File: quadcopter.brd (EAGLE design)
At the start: 185.1 x 185.1 mm, 66 parts, among them J1 AVR_SPI_PRG_6NS, Q1 2.6A, Q2 2.6A, Q3 2.6A, Q4 2.6A, U1 ATMEGA128RFA1, U2 IMU_LSM9DS1TR, Y1 16MHz

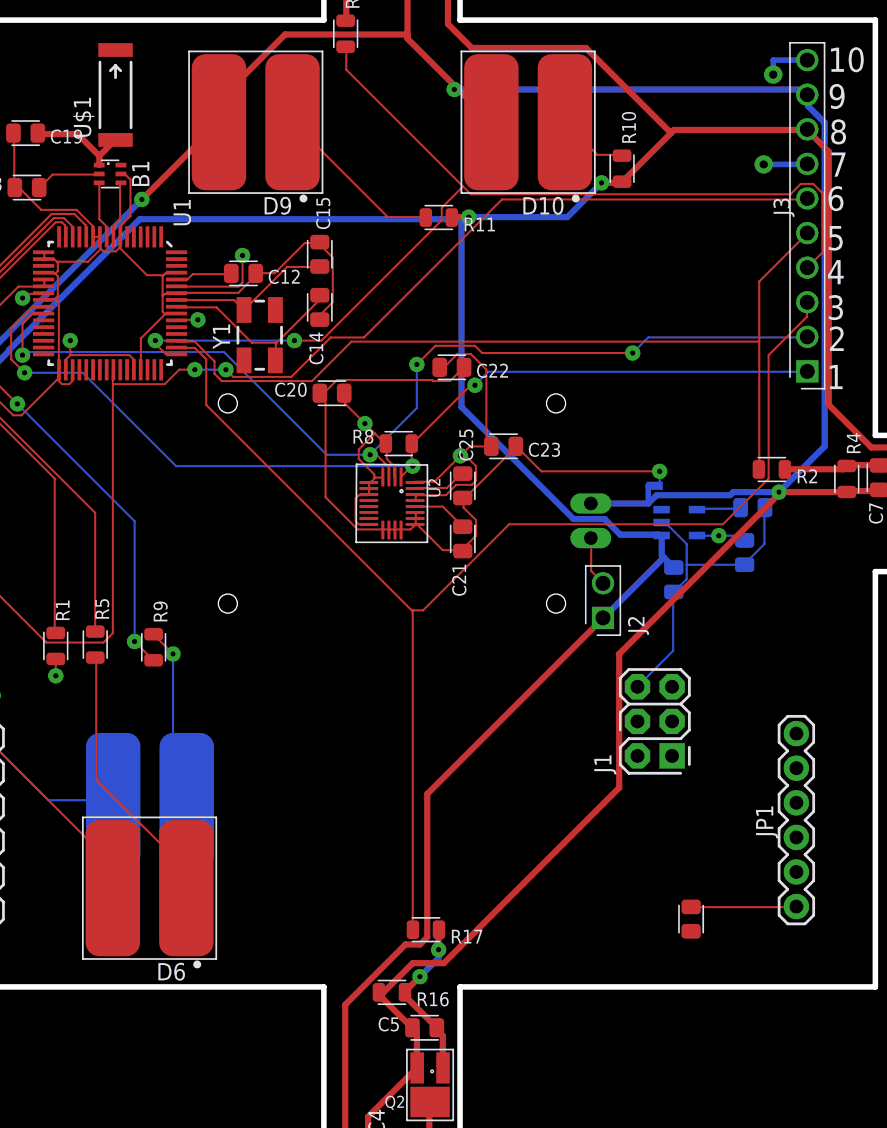
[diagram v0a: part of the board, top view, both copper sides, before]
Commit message: Fixed stop mask errors generated by autorouter
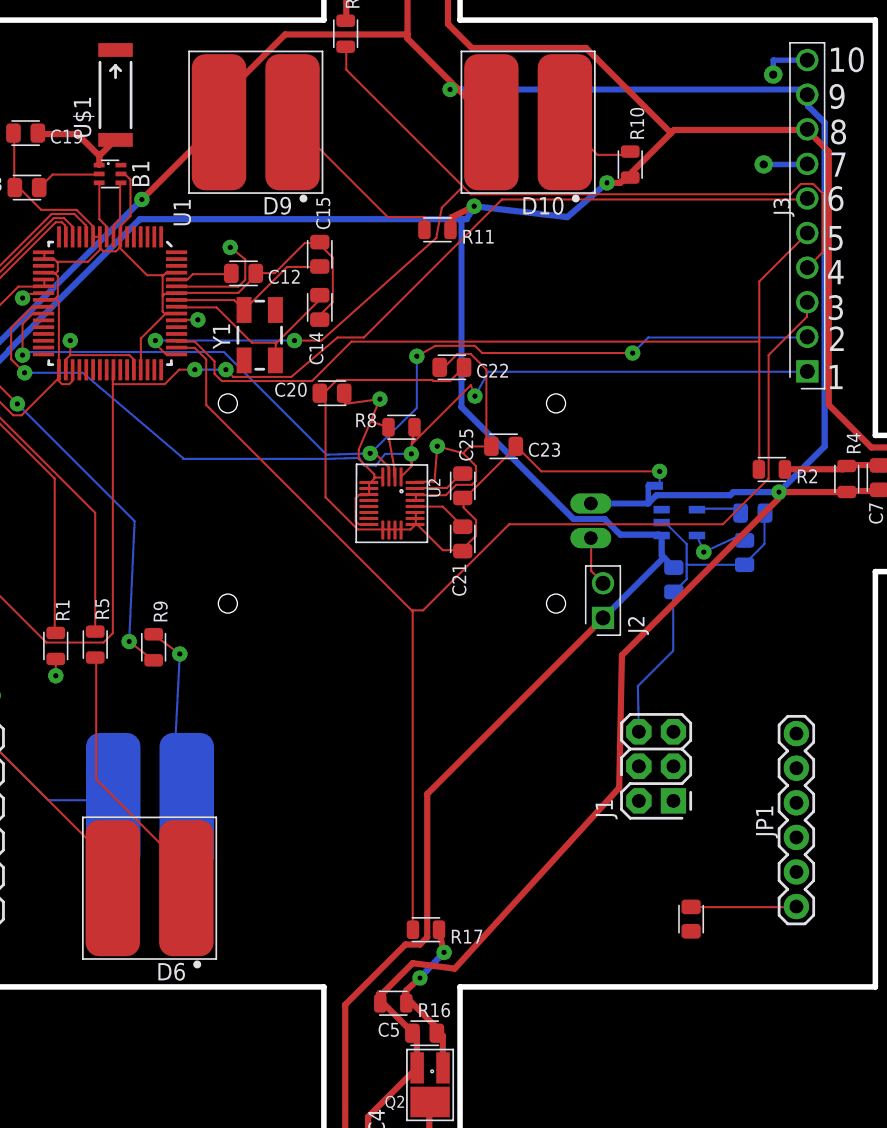
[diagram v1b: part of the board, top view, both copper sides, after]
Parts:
- moved J1 3.30 mm to (19.4, -19.3)
- moved R8 1.22 mm to (0.70, 5.60)
- moved R11 0.91 mm to (3.34, 20.1)
- moved R16 0.81 mm to (0.10, -36.7)
- moved R10 0.67 mm to (17.5, 24.9)
- moved C16 0.40 mm to (26.5, -0.70)
- moved C5 0.40 mm to (2.40, -38.9)
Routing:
- net 3V: track 69.1 -> 76.1 mm
- net SCL: track 72.2 -> 76.6 mm
- net GND: track 195.9 -> 199.6 mm
- net BAT_GND: track 255.6 -> 258.5 mm
- net VBAT: track 319.5 -> 322.3 mm
- net N$34: track 12.3 -> 14.3 mm
- net N$27: track 12.7 -> 13.6 mm
- net N$18: track 5.22 -> 5.84 mm

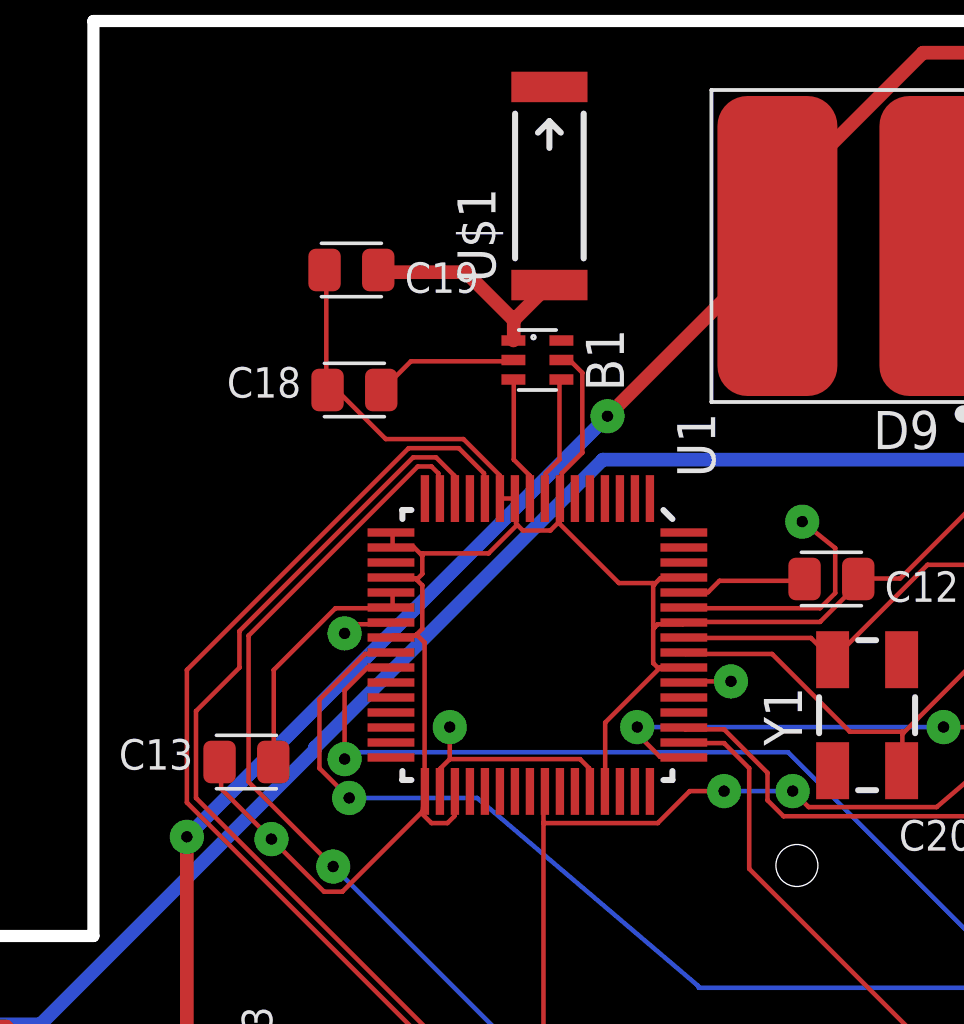
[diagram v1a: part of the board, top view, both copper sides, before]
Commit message: added faraday cage around antenna driver
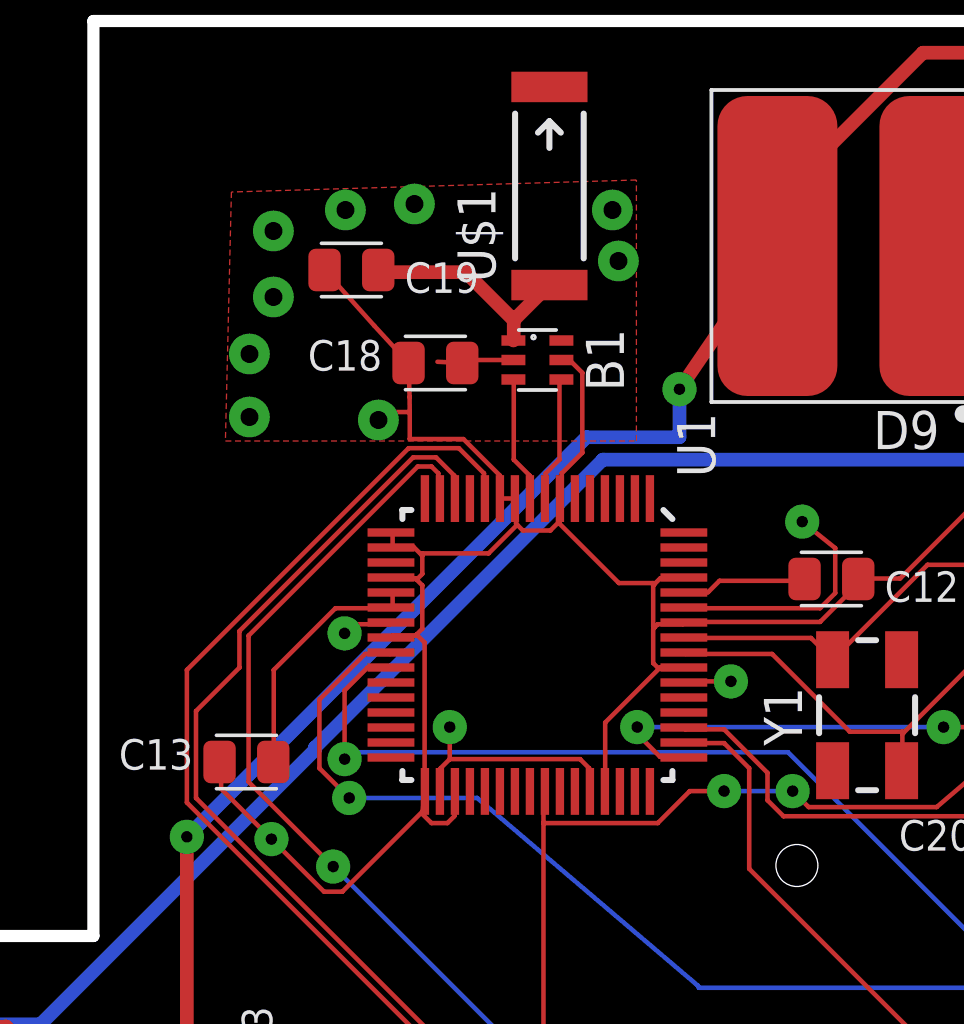
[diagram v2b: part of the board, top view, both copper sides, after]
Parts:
- moved C18 2.85 mm to (-24.1, 24.1)
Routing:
- net N$25: track 4.81 -> 2.63 mm
- net BAT_GND: track 258.5 -> 260.0 mm
- net GND: track 199.6 -> 200.1 mm, vias 4 -> 13
- added copper zone on layer 1, net N$35
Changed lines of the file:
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@@
 <text x="32" y="29" size="1.778" layer="21">9</text>
 <text x="32" y="31.7" size="1.778" layer="21">10</text>
-<polygon width="0.4064" layer="41">
-<vertex x="-34.8" y="33.1"/>
-<vertex x="-17.4" y="32.2"/>
-<vertex x="-17.4" y="28"/>
-<vertex x="-29.1" y="28.6"/>
-<vertex x="-29.1" y="21.5"/>
-<vertex x="-35" y="21.5"/>
-</polygon>
-<polygon width="0.4064" layer="42">
-<vertex x="-17.4" y="32.2"/>
-<vertex x="-17.4" y="28"/>
-<vertex x="-29.1" y="28.6"/>
-<vertex x="-29.1" y="21.4"/>
-<vertex x="-34.9" y="21.4"/>
-<vertex x="-34.8" y="33.1"/>
-</polygon>
-<polygon width="0.4064" layer="41">
-<vertex x="-18.1" y="32.5"/>
-<vertex x="-15.6" y="32.5"/>
-<vertex x="-15.6" y="35"/>
-<vertex x="-18.1" y="35"/>
-</polygon>
-<polygon width="0.4064" layer="41">
-<vertex x="-34.9" y="34.9"/>
-<vertex x="-22.6" y="34.9"/>
-<vertex x="-22.6" y="32.9"/>
-<vertex x="-34.9" y="32.9"/>
-</polygon>
-<polygon width="0.4064" layer="42">
-<vertex x="-18.1" y="35"/>
-<vertex x="-15.5" y="35"/>
-<vertex x="-15.5" y="32.5"/>
-<vertex x="-18.1" y="32.5"/>
-</polygon>
-<polygon width="0.4064" layer="42">
-<vertex x="-34.9" y="34.9"/>
-<vertex x="-22.6" y="34.9"/>
-<vertex x="-22.6" y="32.9"/>
-<vertex x="-34.9" y="32.9"/>
-</polygon>
 </plain>
 <attributes>
@@
 <attribute name="MPN" value="GRM2195C1H103FA01D" x="26.5" y="-0.7" size="1.778" layer="28" rot="MR180" display="off"/>
 </element>
-<element name="C18" library="quadparts_prebuilt" package="CAPC2012X140_HS" value="22pF" x="-26.8" y="23.2" rot="R180">
-<attribute name="DIST" value="Digikey" x="-26.8" y="23.2" size="1.778" layer="27" rot="R180" display="off"/>
-<attribute name="DISTPN" value="490-5534-1-ND" x="-26.8" y="23.2" size="1.778" layer="27" rot="R180" display="off"/>
-<attribute name="MFR" value="Murata Electronics North America" x="-26.8" y="23.2" size="1.778" layer="27" rot="R180" display="off"/>
-<attribute name="MPN" value="GRM21A5C2E220JW01D" x="-26.8" y="23.2" size="1.778" layer="27" rot="R180" display="off"/>
+<element name="C18" library="quadparts_prebuilt" package="CAPC2012X140_HS" value="22pF" x="-24.1" y="24.1" rot="R180">
+<attribute name="DIST" value="Digikey" x="-24.1" y="24.1" size="1.778" layer="27" rot="R180" display="off"/>
+<attribute name="DISTPN" value="490-5534-1-ND" x="-24.1" y="24.1" size="1.778" layer="27" rot="R180" display="off"/>
+<attribute name="MFR" value="Murata Electronics North America" x="-24.1" y="24.1" size="1.778" layer="27" rot="R180" display="off"/>
+<attribute name="MPN" value="GRM21A5C2E220JW01D" x="-24.1" y="24.1" size="1.778" layer="27" rot="R180" display="off"/>
 </element>
 <element name="C19" library="quadparts_prebuilt" package="CAPC2012X140_HS" value="0.75pF" x="-26.9" y="27.2">
@@
 <vertex x="7.5" y="70.6"/>
 <vertex x="-16.4" y="70.6"/>
-<vertex x="-16.9" y="20.8"/>
+<vertex x="-16.5" y="20.8"/>
 </polygon>
 <polygon width="0.4064" layer="2">
-<vertex x="-28.9" y="29.1"/>
-<vertex x="-17.7" y="29.1"/>
-<vertex x="-17.7" y="21.5"/>
-<vertex x="-28.9" y="21.5"/>
+<vertex x="-30.9" y="29.8"/>
+<vertex x="-17.4" y="30.1"/>
+<vertex x="-17.4" y="21.5"/>
+<vertex x="-31.1" y="21.5"/>
 </polygon>
 <wire x1="-31.242" y1="9.906" x2="-31.242" y2="10.7442" width="0.1524" layer="1"/>
@@
 <wire x1="-15.8496" y1="16.9164" x2="-15.819" y2="16.95" width="0.1524" layer="1"/>
 <wire x1="-16.8402" y1="15.3162" x2="-16.8021" y2="15.2781" width="0.1524" layer="1"/>
-<wire x1="-27.7368" y1="23.241" x2="-27.7368" y2="27.1272" width="0.1524" layer="1"/>
+<wire x1="-26.1368" y1="25.341" x2="-27.7368" y2="27.1272" width="0.1524" layer="1"/>
 <wire x1="-27.7368" y1="27.1272" x2="-27.795" y2="27.2" width="0.1524" layer="1"/>
-<wire x1="-27.7368" y1="23.241" x2="-27.695" y2="23.2" width="0.1524" layer="1"/>
+<wire x1="-26.1368" y1="25.341" x2="-24.995" y2="24.1" width="0.1524" layer="1"/>
 <wire x1="-25.527" y1="18.4404" x2="-25.527" y2="17.9832" width="0.1524" layer="1"/>
 <wire x1="-25.527" y1="17.9832" x2="-25.581" y2="17.95" width="0.1524" layer="1"/>
@@
 <wire x1="-21.3741" y1="18.7071" x2="-22.3266" y2="17.7546" width="0.1524" layer="1"/>
 <wire x1="-24.5364" y1="17.7546" x2="-24.5745" y2="17.7165" width="0.1524" layer="1"/>
-<wire x1="-27.3558" y1="23.1648" x2="-27.6606" y2="23.1648" width="0.1524" layer="1"/>
-<wire x1="-25.7556" y1="21.5646" x2="-27.3558" y2="23.1648" width="0.1524" layer="1"/>
-<wire x1="-23.1648" y1="21.5646" x2="-25.7556" y2="21.5646" width="0.1524" layer="1"/>
+<wire x1="-24.9606" y1="22.9648" x2="-24.9558" y2="22.4648" width="0.1524" layer="1"/>
+<wire x1="-24.9556" y1="21.5646" x2="-24.9558" y2="22.4648" width="0.1524" layer="1"/>
+<wire x1="-23.1648" y1="21.5646" x2="-24.9556" y2="21.5646" width="0.1524" layer="1"/>
 <wire x1="-21.9456" y1="20.3454" x2="-23.1648" y2="21.5646" width="0.1524" layer="1"/>
 <wire x1="-21.9456" y1="19.6596" x2="-21.9456" y2="20.3454" width="0.1524" layer="1"/>
-<wire x1="-27.6606" y1="23.1648" x2="-27.695" y2="23.2" width="0.1524" layer="1"/>
+<wire x1="-24.9606" y1="22.9648" x2="-24.995" y2="24.1" width="0.1524" layer="1"/>
 <wire x1="-21.9456" y1="19.6596" x2="-21.95" y2="19.581" width="0.1524" layer="1"/>
 <wire x1="-17.9832" y1="16.764" x2="-16.8402" y2="16.764" width="0.1524" layer="1"/>
@@
 <wire x1="-29.4" y1="-14.1" x2="-29.8" y2="-14" width="0.4064" layer="16"/>
 <wire x1="-29.8" y1="-14" x2="-29.8" y2="-17.2" width="0.4064" layer="16"/>
+<via x="-30.3" y="22.3" extent="1-16" drill="0.6"/>
+<via x="-30.3" y="24.4" extent="1-16" drill="0.6"/>
+<via x="-29.5" y="26.3" extent="1-16" drill="0.6"/>
+<via x="-26" y="22.2" extent="1-16" drill="0.6"/>
+<via x="-18" y="27.5" extent="1-16" drill="0.6"/>
+<via x="-18.2" y="29.2" extent="1-16" drill="0.6"/>
+<via x="-24.8" y="29.4" extent="1-16" drill="0.6"/>
+<via x="-27.1" y="29.2" extent="1-16" drill="0.6"/>
+<via x="-29.5" y="28.5" extent="1-16" drill="0.6"/>
+<wire x1="-24.9558" y1="22.4648" x2="-26" y2="22.4648" width="0.1524" layer="1"/>
+<wire x1="-26" y1="22.4648" x2="-26" y2="22.2" width="0.1524" layer="1"/>
 </signal>
 <signal name="N$2">
@@
 <wire x1="-37.1094" y1="0.6858" x2="-36.95" y2="0.55" width="0.4572" layer="1"/>
 <wire x1="-32.385" y1="8.3058" x2="-32.385" y2="0.1524" width="0.4572" layer="1"/>
-<wire x1="-18.3642" y1="22.3266" x2="-32.385" y2="8.3058" width="0.4572" layer="16"/>
-<wire x1="-12.7254" y1="27.9654" x2="-18.3642" y2="22.3266" width="0.4572" layer="1"/>
+<wire x1="-12.7254" y1="27.9654" x2="-15.9642" y2="23.2266" width="0.4572" layer="1"/>
 <wire x1="-12.7254" y1="27.9654" x2="-12.7" y2="28" width="0.4572" layer="1"/>
 <wire x1="-7.8486" y1="34.4424" x2="1.143" y2="34.4424" width="0.4572" layer="1"/>
@@
 <wire x1="30.3276" y1="30.1752" x2="30.5" y2="30.02" width="0.4572" layer="16"/>
 <via x="-32.385" y="8.3058" extent="1-16" drill="0.381"/>
-<via x="-18.3642" y="22.3266" extent="1-16" drill="0.381"/>
+<via x="-15.9642" y="23.2266" extent="1-16" drill="0.381"/>
 <via x="28.4226" y="0.8382" extent="1-16" drill="0.381"/>
 <via x="4.272" y="30.4038" extent="1-16" drill="0.381"/>
 <wire x1="19" y1="1.3" x2="18.8214" y2="1.3" width="0.4064" layer="16"/>
 <wire x1="18.8214" y1="1.3" x2="18.8214" y2="0" width="0.4064" layer="16"/>
+<wire x1="-15.9642" y1="23.2266" x2="-15.9642" y2="21.6266" width="0.4572" layer="16"/>
+<wire x1="-15.9642" y1="21.6266" x2="-19.0642" y2="21.6266" width="0.4572" layer="16"/>
+<wire x1="-19.0642" y1="21.6266" x2="-32.385" y2="8.3058" width="0.4572" layer="16"/>
 </signal>
 <signal name="VBAT" class="2">
@@
 <vertex x="-7.8" y="34.4"/>
 <vertex x="-16.2" y="34.4"/>
-<vertex x="-16.9" y="20.8"/>
+<vertex x="-16.5" y="20.8"/>
 <vertex x="-34.7" y="20.7"/>
 <vertex x="-34.5" y="7.7"/>
@@
 <contactref element="C18" pad="1"/>
 <contactref element="B1" pad="2"/>
-<wire x1="-24.9174" y1="24.1554" x2="-21.5646" y2="24.1554" width="0.1524" layer="1"/>
-<wire x1="-25.8318" y1="23.241" x2="-24.9174" y2="24.1554" width="0.1524" layer="1"/>
-<wire x1="-21.5646" y1="24.1554" x2="-21.5" y2="24.2" width="0.1524" layer="1"/>
-<wire x1="-25.8318" y1="23.241" x2="-25.905" y2="23.2" width="0.1524" layer="1"/>
+<wire x1="-23.205" y1="24.1" x2="-24.0318" y2="24.141" width="0.1524" layer="1"/>
+<wire x1="-21.5" y1="24.2" x2="-23.205" y2="24.2" width="0.1524" layer="1"/>
+<wire x1="-23.205" y1="24.2" x2="-23.205" y2="24.1" width="0.1524" layer="1"/>
+</signal>
+<signal name="N$35">
+<polygon width="0.4572" layer="1">
+<vertex x="-30.9" y="29.8"/>
+<vertex x="-31.1" y="21.5"/>
+<vertex x="-17.4" y="21.5"/>
+<vertex x="-17.4" y="30.2"/>
+</polygon>
 </signal>
 </signals>

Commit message: Some changes based on design reviews
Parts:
- removed C9: 1uF, quadparts_prebuilt:CAPC2012X140_HS
- added C17: 0.1uF, quadparts_prebuilt:CAPC2012X140_HS
- C3, C5, C7: value 1uF -> 0.1uF
- moved C7 176.5 mm to (-96.5, -115.0), turned to 0 degrees
- moved C3 123.8 mm to (-96.5, -105.4), turned to 0 degrees
- moved C5 121.9 mm to (-96.5, -110.2), turned to 0 degrees
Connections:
- net BAT_GND: now also C10.2, C17.2; no longer C9.2
- net FILTERED: now also C7.1; no longer C9.1
- net GND: no longer C10.2
- net N$31: now also C3.1; no longer C7.1
- net N$33: now also C17.1; no longer C3.1
- net RX0: now also U1.47; no longer U1.46
- net TX0: now also U1.46; no longer U1.47
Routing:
- net BAT_GND: track 260.0 -> 258.8 mm
- net N$34: track 14.3 -> 13.7 mm

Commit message: fixed sch errors
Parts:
- removed C14, C15: 1uF, quadparts_prebuilt:CAPC2012X140_HS
- added C24, C9: 1uF, quadparts_prebuilt:CAPC2012X140_HS
- added C26, C27: 12pF, quadparts_prebuilt:CAPC2012X140_HS
- added R12: 10K, quadparts_prebuilt:RESC2012X60_HS
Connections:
- new net N$36: R12.2, U2.SDA/SDI/SDO
- net 3V: now also C24.1, C9.1, R12.1
- net GND: now also C24.2, C26.2, C27.2, C9.2; no longer C14.2, C15.2
- net N$14: now also C26.1; no longer C14.1
- net N$5: now also C27.1; no longer C15.1
- net SDA: no longer U2.SDA/SDI/SDO
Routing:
- net GND: track 200.0 -> 193.5 mm

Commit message: Fixed board errors
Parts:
- moved C7 181.6 mm to (3.30, 36.7), turned to 90 degrees
- moved C27 178.9 mm to (-9.50, 17.5)
- moved C26 171.4 mm to (-5.20, 11.1), turned to 90 degrees
- moved C3 170.6 mm to (36.3, 1.70), turned to 270 degrees
- moved R12 164.1 mm to (-1.00, 4.20)
- moved C24 148.4 mm to (-20.4, 2.80), turned to 180 degrees
- moved C9 146.5 mm to (-20.4, 5.40), turned to 180 degrees
- moved C5 121.8 mm to (1.90, -38.4), turned to 180 degrees
- moved C17 111.1 mm to (-42.7, -3.40), turned to 180 degrees
- moved D6 43.4 mm to (24.6, -18.9)
- moved JP1 40.3 mm to (-10.6, -29.2), turned to 180 degrees
- moved C1 28.6 mm to (-6.63, -29.2)
- moved D5 7.21 mm to (-20.2, -15.1)
- moved J1 6.20 mm to (13.2, -19.5)
- moved C11 3.26 mm to (26.5, -0.40), turned to 180 degrees
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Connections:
- net BAT_GND: now also D5.C, D6.C; no longer D10.C, D9.C
- net GND: now also D10.C, D9.C; no longer D5.C, D6.C
- net N$18: now also D9.A, R9.2; no longer D10.A, R10.2
- net N$19: now also D10.A, R5.1; no longer D5.A, R9.2
- net N$27: now also D5.A, R10.2; no longer D9.A, R11.1
- net N$28: now also R11.1; no longer R5.1
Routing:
- net VBAT: track 322.3 -> 117.4 mm, vias 3 -> 6
- net BAT_GND: track 258.8 -> 131.2 mm, vias 4 -> 7
- net N$27: track 13.6 -> 90.3 mm, vias 0 -> 1
- net N$19: track 13.6 -> 80.3 mm, vias 1 -> 0
- net 3V: track 76.1 -> 139.0 mm, vias 9 -> 2
- net N$18: track 5.84 -> 44.7 mm
- net PE4: track 95.0 -> 128.1 mm, vias 0 -> 1
- net GND: track 193.5 -> 161.2 mm, vias 13 -> 14
- net N$28: track 19.7 -> 50.2 mm
- net N$24: track 33.7 -> 21.1 mm
- net SCL: track 76.6 -> 66.6 mm, vias 3 -> 2
- net PE3: track 77.1 -> 67.9 mm
- net N$20: track 40.0 -> 31.2 mm, vias 0 -> 2
- net N$26: track 41.8 -> 50.6 mm, vias 2 -> 0
- net SDA: track 73.5 -> 80.3 mm, vias 4 -> 1
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- added copper zone on layer 15, net BAT_GND
